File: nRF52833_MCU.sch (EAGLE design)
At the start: 64 parts, among them IC1 SKY13415-485LF, J1 282834-2, J100 DEBUG_CONNECTOR, J2 282834-2, J3 282834-2, U1 nRF52833-QIAA, U3 BQ25570RGRR, X1 32MHz, X2 32.768kHz, X3 22-23-2031

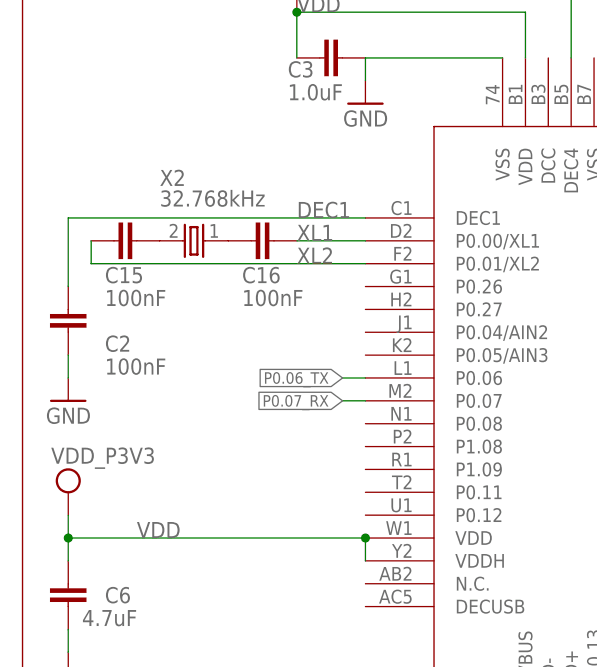
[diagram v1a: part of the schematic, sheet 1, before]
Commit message: GND via for antenna signal
Signed-off-by: Florian Depraz <florian.depraz@outlook.com>
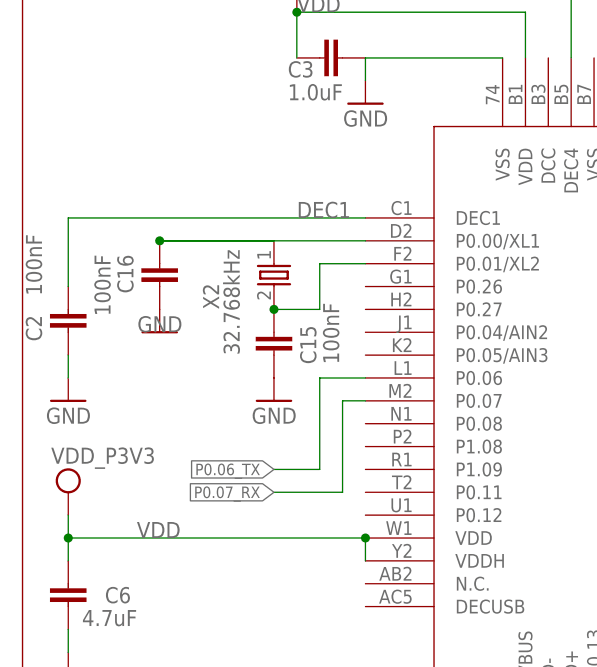
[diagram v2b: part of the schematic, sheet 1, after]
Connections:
- removed net XL1: C16.1, U1.P0.00/XL1
- removed net XL2: C15.1, U1.P0.01/XL2
- net GND: now also C15.1, C16.1
- net N$2: now also U1.P0.00/XL1
- net N$3: now also U1.P0.01/XL2
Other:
- moved on the sheet: C15, C16, X2
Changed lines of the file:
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@@
 <part name="C30" library="Nordic_misc" deviceset="CAPACITOR" device="_0402_N" value="0.7pF"/>
 <part name="C31" library="Nordic_misc" deviceset="CAPACITOR" device="_0402_N" value="N.C."/>
+<part name="GND18" library="supply1" deviceset="GND" device=""/>
+<part name="GND23" library="supply1" deviceset="GND" device=""/>
 </parts>
 <sheets>
@@
 <attribute name="VALUE" x="148.336" y="146.939" size="1.778" layer="96" rot="R180"/>
 </instance>
-<instance part="X2" gate="X$1" x="25.4" y="139.7" smashed="yes" rot="R180">
-<attribute name="NAME" x="20.32" y="145.796" size="1.778" layer="95"/>
-<attribute name="VALUE" x="20.32" y="143.51" size="1.778" layer="96"/>
+<instance part="X2" gate="X$1" x="33.02" y="137.16" smashed="yes" rot="R270">
+<attribute name="NAME" x="26.924" y="132.08" size="1.778" layer="95" rot="R90"/>
+<attribute name="VALUE" x="29.21" y="127" size="1.778" layer="96" rot="R90"/>
 </instance>
 <instance part="J100" gate="G$1" x="154.94" y="53.34" smashed="yes" rot="MR0">
@@
 </instance>
 <instance part="C2" gate="C$1" x="10.16" y="132.08" smashed="yes">
-<attribute name="NAME" x="14.224" y="127.381" size="1.778" layer="95"/>
-<attribute name="VALUE" x="14.224" y="124.841" size="1.778" layer="96"/>
+<attribute name="NAME" x="7.239" y="128.524" size="1.778" layer="95" rot="R90"/>
+<attribute name="VALUE" x="7.239" y="133.604" size="1.778" layer="96" rot="R90"/>
 </instance>
 <instance part="GND1" gate="1" x="10.16" y="121.92" smashed="yes" rot="MR0">
@@
 <attribute name="VALUE" x="247.015" y="154.305" size="1.778" layer="96" rot="R270"/>
 </instance>
-<instance part="C15" gate="C$1" x="15.24" y="139.7" smashed="yes" rot="R90">
-<attribute name="NAME" x="14.224" y="135.001" size="1.778" layer="95"/>
-<attribute name="VALUE" x="14.224" y="132.461" size="1.778" layer="96"/>
-</instance>
-<instance part="C16" gate="C$1" x="33.02" y="139.7" smashed="yes" rot="R270">
-<attribute name="NAME" x="29.464" y="135.001" size="1.778" layer="95"/>
-<attribute name="VALUE" x="29.464" y="132.461" size="1.778" layer="96"/>
+<instance part="C15" gate="C$1" x="33.02" y="127" smashed="yes" rot="R180">
+<attribute name="NAME" x="37.719" y="125.984" size="1.778" layer="95" rot="R90"/>
+<attribute name="VALUE" x="40.259" y="125.984" size="1.778" layer="96" rot="R90"/>
+</instance>
+<instance part="C16" gate="C$1" x="20.32" y="134.62" smashed="yes" rot="R180">
+<attribute name="NAME" x="15.621" y="138.176" size="1.778" layer="95" rot="R270"/>
+<attribute name="VALUE" x="13.081" y="138.176" size="1.778" layer="96" rot="R270"/>
 </instance>
 <instance part="TP11" gate="G$1" x="45.72" y="63.5" smashed="yes">
 <attribute name="NAME" x="44.45" y="64.77" size="1.778" layer="95"/>
 <attribute name="TP_SIGNAL_NAME" x="46.99" y="62.23" size="1.778" layer="97"/>
+</instance>
+<instance part="GND18" gate="1" x="33.02" y="121.92" smashed="yes" rot="MR0">
+<attribute name="VALUE" x="35.56" y="119.38" size="1.778" layer="96" rot="MR0"/>
+</instance>
+<instance part="GND23" gate="1" x="20.32" y="129.54" smashed="yes" rot="MR0">
+<attribute name="VALUE" x="22.86" y="129.54" size="1.778" layer="96" rot="MR0"/>
 </instance>
 </instances>
@@
 <net name="P0.06_TX" class="0">
 <segment>
-<label x="40.64" y="124.46" size="1.27" layer="95" rot="R180" xref="yes"/>
-<wire x1="43.18" y1="124.46" x2="40.64" y2="124.46" width="0.1524" layer="91"/>
+<label x="33.02" y="114.3" size="1.27" layer="95" rot="R180" xref="yes"/>
+<wire x1="43.18" y1="124.46" x2="38.1" y2="124.46" width="0.1524" layer="91"/>
+<wire x1="38.1" y1="124.46" x2="38.1" y2="114.3" width="0.1524" layer="91"/>
+<wire x1="38.1" y1="114.3" x2="33.02" y2="114.3" width="0.1524" layer="91"/>
 <pinref part="U1" gate="A" pin="P0.06"/>
 </segment>
@@
 <net name="P0.07_RX" class="0">
 <segment>
-<label x="40.64" y="121.92" size="1.27" layer="95" rot="R180" xref="yes"/>
+<label x="33.02" y="111.76" size="1.27" layer="95" rot="R180" xref="yes"/>
 <wire x1="43.18" y1="121.92" x2="40.64" y2="121.92" width="0.1524" layer="91"/>
+<wire x1="40.64" y1="121.92" x2="40.64" y2="111.76" width="0.1524" layer="91"/>
+<wire x1="40.64" y1="111.76" x2="33.02" y2="111.76" width="0.1524" layer="91"/>
 <pinref part="U1" gate="A" pin="P0.07"/>
 </segment>
@@
 <junction x="142.24" y="154.94"/>
 <label x="127" y="142.24" size="1.778" layer="95"/>
-</segment>
-</net>
-<net name="XL1" class="0">
-<segment>
-<pinref part="U1" gate="A" pin="P0.00/XL1"/>
-<wire x1="43.18" y1="139.7" x2="35.56" y2="139.7" width="0.1524" layer="91"/>
-<label x="35.56" y="139.7" size="1.778" layer="95"/>
-<pinref part="C16" gate="C$1" pin="1"/>
-</segment>
-</net>
-<net name="XL2" class="0">
-<segment>
-<pinref part="U1" gate="A" pin="P0.01/XL2"/>
-<wire x1="12.7" y1="137.16" x2="43.18" y2="137.16" width="0.1524" layer="91"/>
-<label x="35.56" y="137.16" size="1.778" layer="95"/>
-<pinref part="C15" gate="C$1" pin="1"/>
-<wire x1="12.7" y1="137.16" x2="12.7" y2="139.7" width="0.1524" layer="91"/>
 </segment>
 </net>
@@
 <wire x1="10.16" y1="124.46" x2="10.16" y2="127" width="0.1524" layer="91"/>
 </segment>
+<segment>
+<pinref part="GND18" gate="1" pin="GND"/>
+<pinref part="C15" gate="C$1" pin="1"/>
+</segment>
+<segment>
+<pinref part="GND23" gate="1" pin="GND"/>
+<pinref part="C16" gate="C$1" pin="1"/>
+</segment>
 </net>
 <net name="N$8" class="0">
@@
 <pinref part="X2" gate="X$1" pin="1"/>
 <pinref part="C16" gate="C$1" pin="2"/>
-</segment>
-</net>
-<net name="N$3" class="0">
-<segment>
-<pinref part="X2" gate="X$1" pin="2"/>
-<pinref part="C15" gate="C$1" pin="2"/>
+<wire x1="20.32" y1="139.7" x2="33.02" y2="139.7" width="0.1524" layer="91"/>
+<pinref part="U1" gate="A" pin="P0.00/XL1"/>
+<wire x1="20.32" y1="139.7" x2="43.18" y2="139.7" width="0.1524" layer="91"/>
+<junction x="20.32" y="139.7"/>
 </segment>
 </net>
@@
 </segment>
 </net>
+<net name="N$3" class="0">
+<segment>
+<pinref part="X2" gate="X$1" pin="2"/>
+<pinref part="C15" gate="C$1" pin="2"/>
+<pinref part="U1" gate="A" pin="P0.01/XL2"/>
+<wire x1="38.1" y1="137.16" x2="43.18" y2="137.16" width="0.1524" layer="91"/>
+<wire x1="38.1" y1="137.16" x2="38.1" y2="132.08" width="0.1524" layer="91"/>
+<wire x1="33.02" y1="132.08" x2="38.1" y2="132.08" width="0.1524" layer="91"/>
+<junction x="33.02" y="132.08"/>
+</segment>
+</net>

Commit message: Fix warnings
Signed-off-by: Florian Depraz <florian.depraz@outlook.com>
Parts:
- removed C14, C26, C29: NC, Nordic_misc:CAPACITOR_0402_N
- removed C23: 0.01uF, Nordic_misc:CAPACITOR_0402_N
- removed C24, C27: 0.1uF, Nordic_misc:CAPACITOR_0402_N
- removed C25, C28: 4.7uF, Nordic_misc:CAPACITOR_0402_N
- removed J1, J2: 282834-2, 282834-2:282834-2
- removed L1, L2: DR73-220-R, DR73-220-R:DR73-220-R
- removed R11: 0.05R, Y14870RXX000B9R:Y14870RXX000B9R
- removed SJ2: (no value), jumper:SJ
- removed TP1, TP11, TP2, TP3, TP4, TP5, TP6, TP7: TPPAD1-13, testpad:TPPAD1-13
- removed U3: BQ25570RGRR, BQ25570RGRR:BQ25570RGRR
- added C18: 1.0pF, Nordic_misc:CAPACITOR_0402_N
- added C32: 1.2pF, Nordic_misc:CAPACITOR_0402_N
- added L8: 2.2nH, Nordic_misc:INDUCTOR_0402_N
- added L9: 4.7nH, Nordic_misc:INDUCTOR_0402_N
- ANT1, ANT2: value ANTENNA_QUARTER-WAVE_MONOPOLE_MEANDERED_LEFT -> 2450AT18B100E; device Nordic_misc:ANTENNA_QUARTER-WAVE_MONOPOLE_MEANDERED_LEFT -> 2450AT18B100E:2450AT18B100E
- ANT4, ANT5: value SWRA092B -> 2450AT18B100E; device texas:SWRA092B -> 2450AT18B100E:2450AT18B100E
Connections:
- removed net BQ_EXT_VBAT: J1.2, TP6.TP, U3.VBAT
- removed net BQ_LBUCK: L1.2, TP7.TP, U3.LBUCK
- removed net BQ_NEN: TP11.TP, U1.P0.15, U3.!EN
- removed net BQ_RSP1: J2.2, R11.2, SJ2.2
- removed net BQ_SUPPLY_VBAT: C14.1, L1.1, X3-3.S
- removed net BQ_VBAT_OK: U1.D-, U3.VBAT_OK
- removed net BQ_VBAT_OV: TP2.TP, U3.VBAT_OV
- removed net BQ_VIN_DC: C27.1, C28.1, C29.1, L2.1, R11.1, SJ2.1, U3.VIN_DC
- removed net BQ_VOUT: U3.VOUT
- removed net BQ_VOUT_EN: TP4.TP, U3.VOUT_EN
- removed net BQ_VOUT_SET: TP5.TP, U3.VOUT_SET
- removed net BQ_VRDIV: U3.VRDIV
- removed net BQ_VSTOR: C24.1, C25.1, C26.1, U3.VSTOR
- removed net LBOOST: L2.2, U3.LBOOST
- removed net N$18: TP1.TP
- removed net VOC_SAMP: TP3.TP, U3.VOC_SAMP
- removed net VREF_SAMP: C23.1, U3.VREF_SAMP
- new net N$22: IC1.ANT, L8.2
- new net N$23: C32.1, L8.1, L9.2
- net GND: now also C18.2, C32.2; no longer C14.2, C23.2, C24.2, C25.2, C26.2, C27.2, C28.2, C29.2, J1.1, J2.1, U3.EP@1, U3.EP@2, U3.EP@3, U3.EP@4, U3.EP@5, U3.NC1, U3.NC2, U3.OK_HYST, U3.OK_PROG, U3.VSS@1, U3.VSS@2
- net N$13: now also ANT4.FEED; no longer ANT5.ANTENNA
- net N$14: now also ANT5.FEED; no longer ANT4.ANTENNA
- net N$40: now also ANT2.FEED; no longer ANT2.P$1
- net N$5: now also ANT1.FEED; no longer ANT1.P$1
- net NRF_ANT: now also C18.1, L9.1; no longer IC1.ANT
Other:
- note added: "UFL connector"
- note removed: "22uF"
- note removed: "DC voltage input from energy harvesting source (Solar,..)"
- note removed: "Lithium Battery At least 100uF for storage"
- note removed: "Select supply source"
- moved on the sheet: ANT3, C10, C13, C17, C19, C20, C21, C22, C30, C31, IC1, J3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

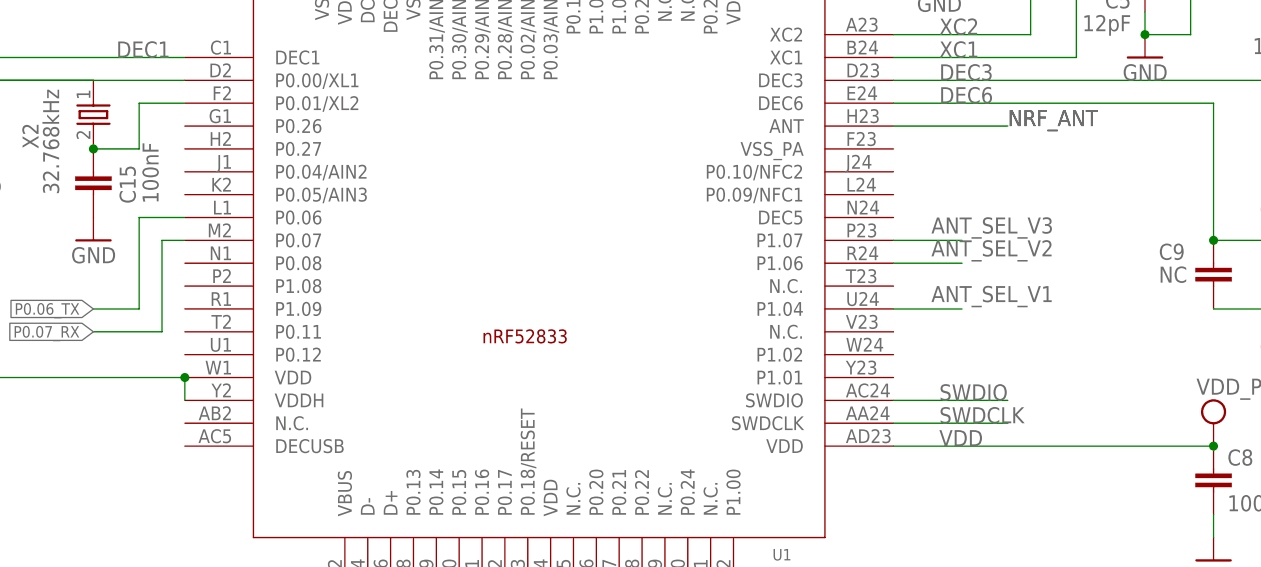
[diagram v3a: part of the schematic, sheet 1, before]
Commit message: Fix pad/signal spacing issue
Signed-off-by: Florian Depraz <florian.depraz@outlook.com>
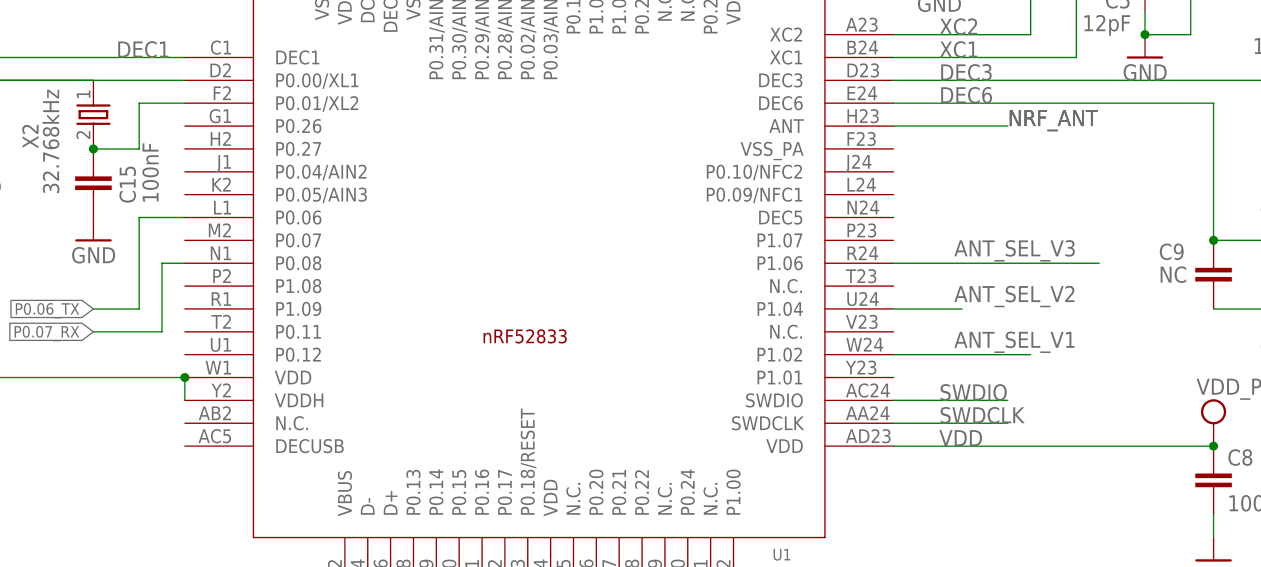
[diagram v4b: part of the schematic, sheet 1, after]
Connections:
- net ANT_SEL_V1: now also U1.P1.02; no longer U1.P1.04
- net ANT_SEL_V2: now also U1.P1.04; no longer U1.P1.06
- net ANT_SEL_V3: now also U1.P1.06; no longer U1.P1.07
- net P0.07_RX: now also U1.P0.08; no longer U1.P0.07
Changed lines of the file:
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@@
 <segment>
 <label x="33.02" y="111.76" size="1.27" layer="95" rot="R180" xref="yes"/>
-<wire x1="43.18" y1="121.92" x2="40.64" y2="121.92" width="0.1524" layer="91"/>
-<wire x1="40.64" y1="121.92" x2="40.64" y2="111.76" width="0.1524" layer="91"/>
+<wire x1="40.64" y1="119.38" x2="40.64" y2="111.76" width="0.1524" layer="91"/>
 <wire x1="40.64" y1="111.76" x2="33.02" y2="111.76" width="0.1524" layer="91"/>
-<pinref part="U1" gate="A" pin="P0.07"/>
+<pinref part="U1" gate="A" pin="P0.08"/>
+<wire x1="43.18" y1="119.38" x2="40.64" y2="119.38" width="0.1524" layer="91"/>
 </segment>
 <segment>
@@
 <net name="ANT_SEL_V1" class="0">
 <segment>
-<wire x1="121.92" y1="114.3" x2="129.54" y2="114.3" width="0.1524" layer="91"/>
-<label x="139.7" y="116.84" size="1.778" layer="95" rot="R180"/>
+<label x="142.24" y="111.76" size="1.778" layer="95" rot="R180"/>
+<pinref part="U1" gate="A" pin="P1.02"/>
+<wire x1="137.16" y1="109.22" x2="121.92" y2="109.22" width="0.1524" layer="91"/>
+</segment>
+</net>
+<net name="ANT_SEL_V2" class="0">
+<segment>
+<label x="142.24" y="116.84" size="1.778" layer="95" rot="R180"/>
 <pinref part="U1" gate="A" pin="P1.04"/>
-</segment>
-</net>
-<net name="ANT_SEL_V2" class="0">
-<segment>
-<wire x1="121.92" y1="119.38" x2="129.54" y2="119.38" width="0.1524" layer="91"/>
-<label x="139.7" y="121.92" size="1.778" layer="95" rot="R180"/>
+<wire x1="129.54" y1="114.3" x2="121.92" y2="114.3" width="0.1524" layer="91"/>
+</segment>
+</net>
+<net name="ANT_SEL_V3" class="0">
+<segment>
+<label x="142.24" y="121.92" size="1.778" layer="95" rot="R180"/>
 <pinref part="U1" gate="A" pin="P1.06"/>
-</segment>
-</net>
-<net name="ANT_SEL_V3" class="0">
-<segment>
-<wire x1="121.92" y1="121.92" x2="129.54" y2="121.92" width="0.1524" layer="91"/>
-<label x="139.7" y="124.46" size="1.778" layer="95" rot="R180"/>
-<pinref part="U1" gate="A" pin="P1.07"/>
+<wire x1="121.92" y1="119.38" x2="144.78" y2="119.38" width="0.1524" layer="91"/>
 </segment>
 </net>
@@
 <pinref part="ANT4" gate="G$1" pin="FEED"/>
 <junction x="200.66" y="124.46"/>
-<pinref part="ANT4" gate="G$1" pin="FEED"/>
 </segment>
 </net>
@@
 <pinref part="ANT5" gate="G$1" pin="FEED"/>
 <junction x="200.66" y="86.36"/>
-<pinref part="ANT5" gate="G$1" pin="FEED"/>
-</segment>
-</net>
+</segment>
+</net>
